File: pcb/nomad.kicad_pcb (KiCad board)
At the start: 2 copper layers, 61 x 142 mm, 79 parts, among them J1 USB_C_Receptacle_USB2.0_16P, J2 Conn_01x08_Pin, J3 Conn_Coaxial, J4 Conn_Coaxial, J5 Conn_01x02_Pin, J6 Conn_01x03_Socket, Q2 2N7002, SW1 UP, SW2 DOWN, SW3 RIGHT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

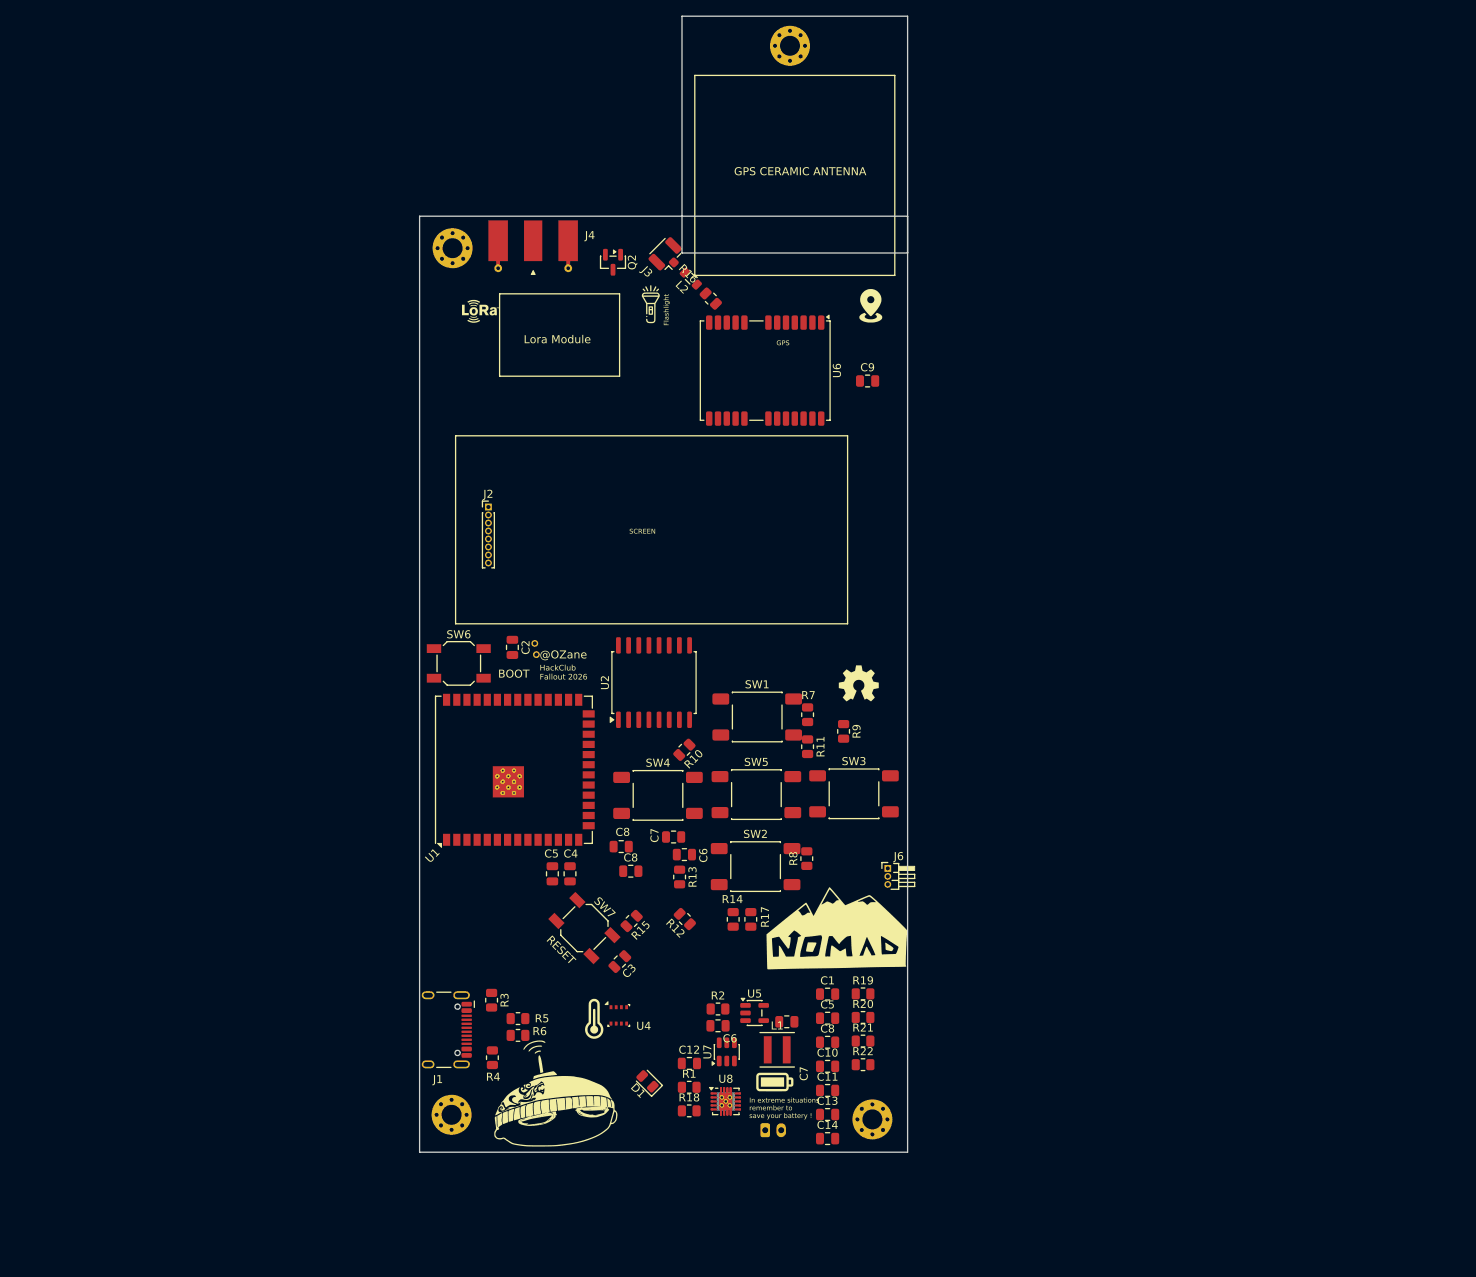
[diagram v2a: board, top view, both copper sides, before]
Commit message: Updating PCB and chainging pin for the LoRa module
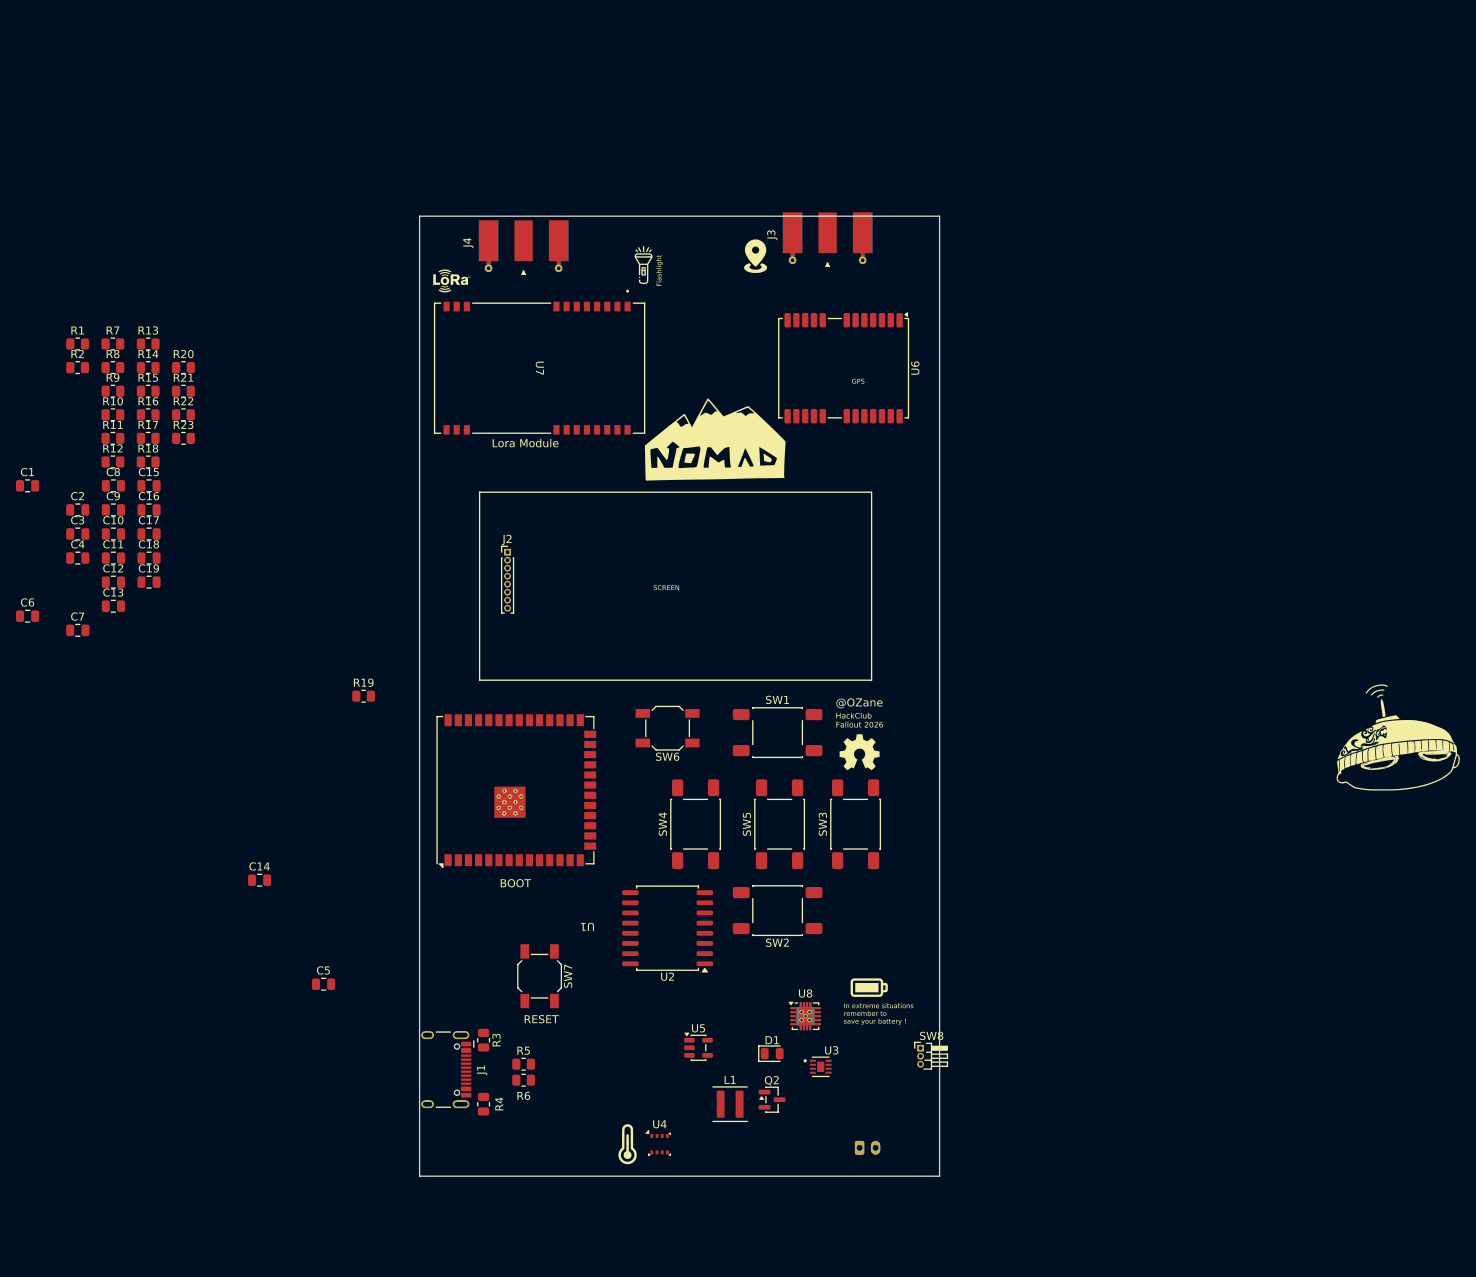
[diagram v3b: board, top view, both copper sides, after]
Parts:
- removed ? (x2): , 
- removed the C5 at (116.6, 127.2)
- removed the C5 at (151.0, 145.2)
- removed the C6 at (133.1, 124.8)
- removed the C6 at (137.3, 146.2)
- removed the C7 at (145.9, 145.7)
- removed the C7 at (131.8, 122.6)
- removed the C8 at (126.4, 126.9)
- removed the C8 at (151.0, 148.3)
- removed the C8 at (125.2, 123.8)
- removed J6: Conn_01x03_Socket, Connector_PinHeader_1.00mm:PinHeader_1x03_P1.00mm_Horizontal
- removed L2: 27nH, Inductor_SMD:L_0805_2012Metric
- removed REF** (x4): MountingHole_2.5mm_Pad_Via, MountingHole:MountingHole_2.5mm_Pad_Via
- added C15: 0.1uF, Capacitor_SMD:C_0805_2012Metric, F.Cu at (66.2, 78.7)
- added C16: 0.1uF, Capacitor_SMD:C_0805_2012Metric, F.Cu at (66.2, 81.7)
- added C17: 10uF, Capacitor_SMD:C_0805_2012Metric, F.Cu at (66.2, 84.7)
- added C18: 0.1uF, Capacitor_SMD:C_0805_2012Metric, F.Cu at (66.2, 87.7)
- added C19: 10uF, Capacitor_SMD:C_0805_2012Metric, F.Cu at (66.2, 90.7)
- added C5: 22uF, Capacitor_SMD:C_0805_2012Metric, F.Cu at (88.0, 141.0)
- added C6: C, Capacitor_SMD:C_0805_2012Metric, F.Cu at (51.0, 95.0)
- added C7: 4.7uF, Capacitor_SMD:C_0805_2012Metric, F.Cu at (57.3, 96.8)
- added C8: 0.1uF, Capacitor_SMD:C_0805_2012Metric, F.Cu at (61.7, 78.7)
- added R23: 1K, Resistor_SMD:R_0805_2012Metric, F.Cu at (70.5, 72.8)
- added SW8: SW_SPDT, Connector_PinHeader_1.00mm:PinHeader_1x03_P1.00mm_Horizontal, F.Cu at (162.6, 149.0)
- added U3: MAX17048G_T10, MAX17048G_T10:SON50P200X200X80-9N, F.Cu at (150.1, 151.3)
- C9: value 47pF -> 0.1uF
- J3: footprint Connector_Coaxial:U.FL_Hirose_U.FL-R-SMT-1_Vertical -> Connector_Coaxial:SMA_Molex_73251-1153_EdgeMount_Horizontal
- R16: value 10R -> 10k
- U7: value DW01A -> E220-900T22S; footprint Package_TO_SOT_SMD:SOT-23-6 -> footprints:E220-900T22S_BYT
- moved R1 120.3 mm to (57.3, 61.0)
- moved C1 118.5 mm to (51.0, 78.7)
- moved R20 117.5 mm to (70.5, 63.9)
- moved R21 117.5 mm to (70.5, 66.9)
- moved R22 117.5 mm to (70.5, 69.8)
- moved G*** 114.3 mm to (236.5, 157.8)
- moved R2 113.3 mm to (57.3, 63.9)
- moved C10 111.3 mm to (61.7, 84.7)
- moved C11 111.3 mm to (61.7, 87.7)
- moved C13 109.6 mm to (61.7, 93.8)
- moved Q2 106.6 mm to (144.1, 155.4), turned to 0 degrees
- moved R8 106.3 mm to (61.7, 63.9), turned to 0 degrees
- moved R18 105.6 mm to (66.1, 75.7)
- moved R9 100.7 mm to (61.7, 66.9), turned to 0 degrees
- moved R14 100.5 mm to (66.1, 63.9), turned to 0 degrees
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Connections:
- net SWBAT+ renamed Net-(SW8-A)
- C14 pad 2: Net-(U8-VOUT) -> +3V3
- C9 pad 1: GND -> +3V3
- C9 pad 2: Net-(C9-Pad2) -> GND
- D1 pad 2: +3V3 -> +5V
- J2 pad 1: BLK -> +3V3
- J4 pad 1: unconnected-(J4-In-Pad1) -> Net-(J4-In)
- J5 pad 1: +BATT -> Net-(J5-Pin_1)
- R16 pad 1: Net-(C9-Pad2) -> Net-(U6-D_SEL)
- R16 pad 2: Net-(U6-VCC_RF) -> +3V3
- R2 pad 1: GND -> Net-(U5-PROG)
- R2 pad 2: Net-(U5-V_{SS}) -> GND
- R20 pad 2: Net-(U8-VOUT) -> +3V3
- R21 pad 1: Net-(U8-VOUT) -> +3V3
- U1 pad 10: unconnected-(U1-IO17-Pad10) -> GPS MI
- U1 pad 11: unconnected-(U1-IO18-Pad11) -> AUX
- U1 pad 23: unconnected-(U1-IO21-Pad23) -> LORA_MI
- U1 pad 24: unconnected-(U1-IO47-Pad24) -> LORA_MO
- U1 pad 9: unconnected-(U1-IO16-Pad9) -> GPS MO
- U4 pad 2: unconnected-(U4-CSB-Pad2) -> Net-(U4-CSB)
- U5 pad 2: Net-(U5-V_{SS}) -> GND
- U5 pad 4: +3V3 -> +5V
- U5 pad 5: GND -> Net-(U5-PROG)
- U6 pad 2: unconnected-(U6-D_SEL-Pad2) -> Net-(U6-D_SEL)
- U6 pad 7: unconnected-(U6-VDD_USB-Pad7) -> GND
- U6 pad 9: Net-(U6-VCC_RF) -> unconnected-(U6-VCC_RF-Pad9)
- U7 pad 2: unconnected-(U7-CS-Pad2) -> GND
- U8 pad 9: Net-(U8-VOUT) -> +3V3
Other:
- board size 61 x 142 mm -> 65 x 120 mm
- board text removed: "GPS CERAMIC ANTENNA"

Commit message: Finishing schematic and updating PCB
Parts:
- removed C11: C, Capacitor_SMD:C_0805_2012Metric
- added D2: LED, LED_SMD:LED_Cree-XP-G, B.Cu at (132.0, 50.0)
- added REF**: MountingHole_2.2mm_M2_Pad_Via, MountingHole:MountingHole_2.2mm_M2_Pad_Via, F.Cu at (162.0, 48.0)
- added REF**: MountingHole_2.2mm_M2_Pad_Via, MountingHole:MountingHole_2.2mm_M2_Pad_Via, F.Cu at (107.0, 161.5)
- added REF**: MountingHole_2.2mm_M2_Pad_Via, MountingHole:MountingHole_2.2mm_M2_Pad_Via, F.Cu at (161.8, 162.0)
- added REF**: MountingHole_2.2mm_M2_Pad_Via, MountingHole:MountingHole_2.2mm_M2_Pad_Via, F.Cu at (103.7, 48.8)
- C1: value C -> 0.1uF
- C10: value C -> 22uF
- moved R14 115.7 mm to (161.0, 130.0), turned to -90 degrees
- moved R17 113.0 mm to (163.5, 130.0), turned to 90 degrees
- moved C15 112.9 mm to (162.6, 137.5)
- moved R2 111.9 mm to (125.0, 153.0)
- moved C16 107.4 mm to (158.0, 137.5), turned to 180 degrees
- moved R23 101.2 mm to (155.0, 128.5)
- moved Q2 100.1 mm to (133.0, 55.9), turned to 90 degrees
- moved C9 98.2 mm to (159.5, 73.0)
- moved R13 96.2 mm to (123.0, 138.5), turned to 90 degrees
- moved R18 95.0 mm to (122.0, 152.5), turned to -90 degrees
- moved R16 94.6 mm to (159.5, 55.0)
- moved R21 94.5 mm to (115.9, 149.8), turned to 180 degrees
- moved C17 93.8 mm to (159.5, 75.5)
- moved C7 93.0 mm to (129.0, 156.0), turned to 90 degrees
- moved C6 92.8 mm to (120.0, 157.0), turned to 90 degrees
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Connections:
- C5 pad 2: Net-(SW8-A) -> Net-(SW8-C)
- J5 pad 1: Net-(J5-Pin_1) -> +BATT
- J5 pad 2: -BATT -> GND
- SW8 pad 1: Net-(SW8-A) -> unconnected-(SW8-A-Pad1)
- SW8 pad 2: Net-(J5-Pin_1) -> +BATT
- SW8 pad 3: unconnected-(SW8-C-Pad3) -> Net-(SW8-C)
- U1 pad 36: UART_TX -> unconnected-(U1-RXD0-Pad36)
- U8 pad 2: Net-(SW8-A) -> Net-(SW8-C)
- U8 pad 3: Net-(SW8-A) -> Net-(SW8-C)
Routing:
- net Net-(J1-D+-PadA6): track 0.00 -> 7.51 mm
- net Net-(J1-D--PadA7): track 0.00 -> 7.30 mm
- net Net-(J1-CC2): track 0.00 -> 4.37 mm
- net (no net): vias 0 -> 53
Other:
- board text removed: "Flashlight"

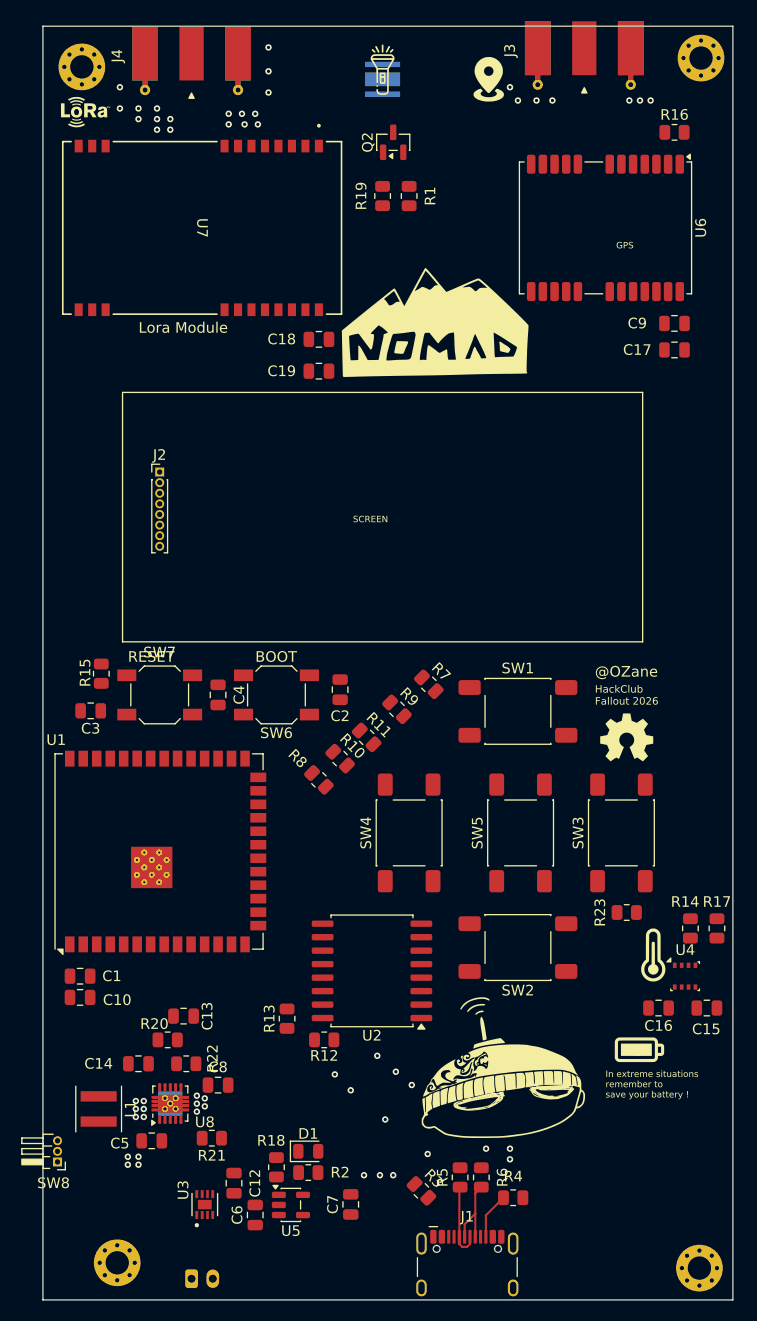
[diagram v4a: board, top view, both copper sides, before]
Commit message: Routing the PCB
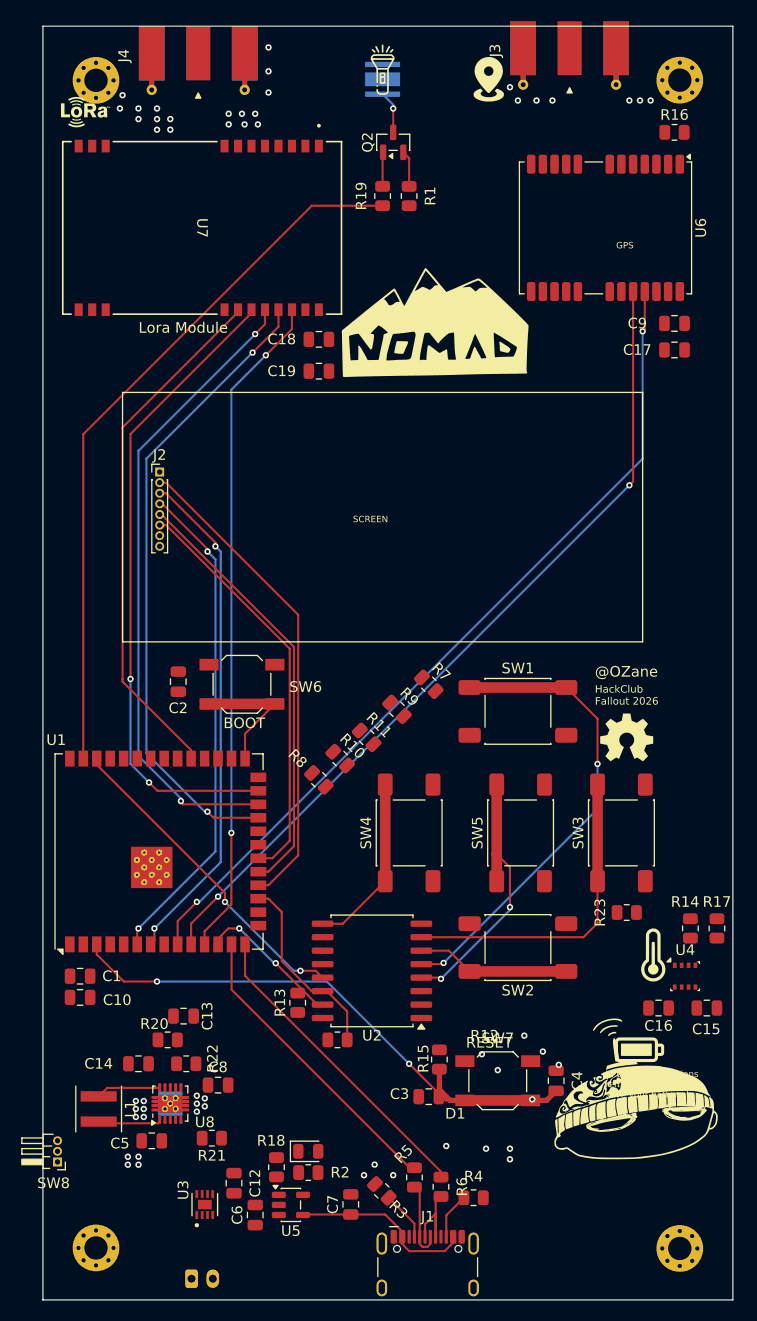
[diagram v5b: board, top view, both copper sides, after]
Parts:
- C13: value 10uF -> 10pF
- moved C3 48.3 mm to (136.3, 145.9)
- moved C4 48.3 mm to (148.3, 144.4)
- moved R15 48.3 mm to (137.3, 142.4)
- moved SW7 48.3 mm to (142.8, 144.4)
- moved C2 15.3 mm to (112.8, 106.8)
- moved G*** 12.7 mm to (170.1, 192.8)
- moved R5 4.30 mm to (135.0, 153.5)
- moved R6 3.90 mm to (137.5, 154.3)
- moved R4 3.73 mm to (140.6, 155.4)
- moved J1 3.73 mm to (136.2, 162.8)
- moved R3 3.73 mm to (131.9, 154.7)
- moved SW6 3.40 mm to (118.8, 107.0)
- moved REF** 2.89 mm to (160.0, 50.1)
- moved REF** 2.62 mm to (160.0, 160.2)
- moved REF** 2.44 mm to (105.0, 160.1)
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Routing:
- net GPS MO: track 0.00 -> 79.9 mm, vias 0 -> 2
- net GPS MI: track 0.00 -> 78.7 mm, vias 0 -> 2
- net FLASHLIGHT: track 0.00 -> 67.7 mm
- net AUX: track 0.00 -> 63.2 mm, vias 0 -> 2
- net M1: track 0.00 -> 60.6 mm, vias 0 -> 2
- net LORA_MO: track 0.00 -> 60.4 mm, vias 0 -> 2
- net LORA_MI: track 0.00 -> 60.0 mm, vias 0 -> 2
- net RESET: track 0.00 -> 53.6 mm, vias 0 -> 3
- net M0: track 0.00 -> 49.5 mm
- net DC: track 0.00 -> 48.0 mm, vias 0 -> 2
- net RES: track 0.00 -> 46.9 mm, vias 0 -> 2
- net CS: track 0.00 -> 45.8 mm
- net BTN_UP: track 0.00 -> 44.4 mm, vias 0 -> 2
- net MOSI: track 0.00 -> 40.9 mm
- net SCLK: track 0.00 -> 38.8 mm
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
